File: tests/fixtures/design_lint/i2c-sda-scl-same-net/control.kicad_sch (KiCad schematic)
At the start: 1 part, among them U1 I2C controller

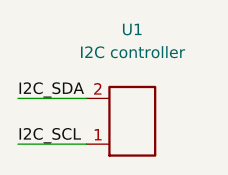
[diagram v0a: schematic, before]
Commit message: fix: align same-net native control fixtures
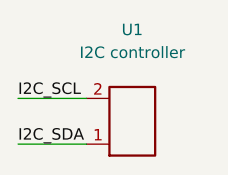
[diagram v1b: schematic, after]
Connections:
- net I2C_SCL: now also U1.2 (SCL); no longer U1.1 (SDA)
- net I2C_SDA: now also U1.1 (SDA); no longer U1.2 (SCL)
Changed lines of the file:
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@@
   (wire (pts (xy 58.42 60.96) (xy 50.80 60.96))
     (stroke (width 0) (type default)))
-  (label "I2C_SDA" (at 50.80 60.96 0)
+  (label "I2C_SCL" (at 50.80 60.96 0)
     (effects (font (size 1.27 1.27)) (justify left bottom))
 )
   (wire (pts (xy 58.42 66.04) (xy 50.80 66.04))
     (stroke (width 0) (type default)))
-  (label "I2C_SCL" (at 50.80 66.04 0)
+  (label "I2C_SDA" (at 50.80 66.04 0)
     (effects (font (size 1.27 1.27)) (justify left bottom))
 )
